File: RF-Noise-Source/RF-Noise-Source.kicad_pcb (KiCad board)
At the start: 2 copper layers, 44 parts, among them J1 Conn_01x02_Male, J2 Conn_Coaxial, Q1 J310, Q2 J310, U1 OPA842xDBV, U2 OPA842xDBV, U3 OPA842xDBV, U4 TPS76350

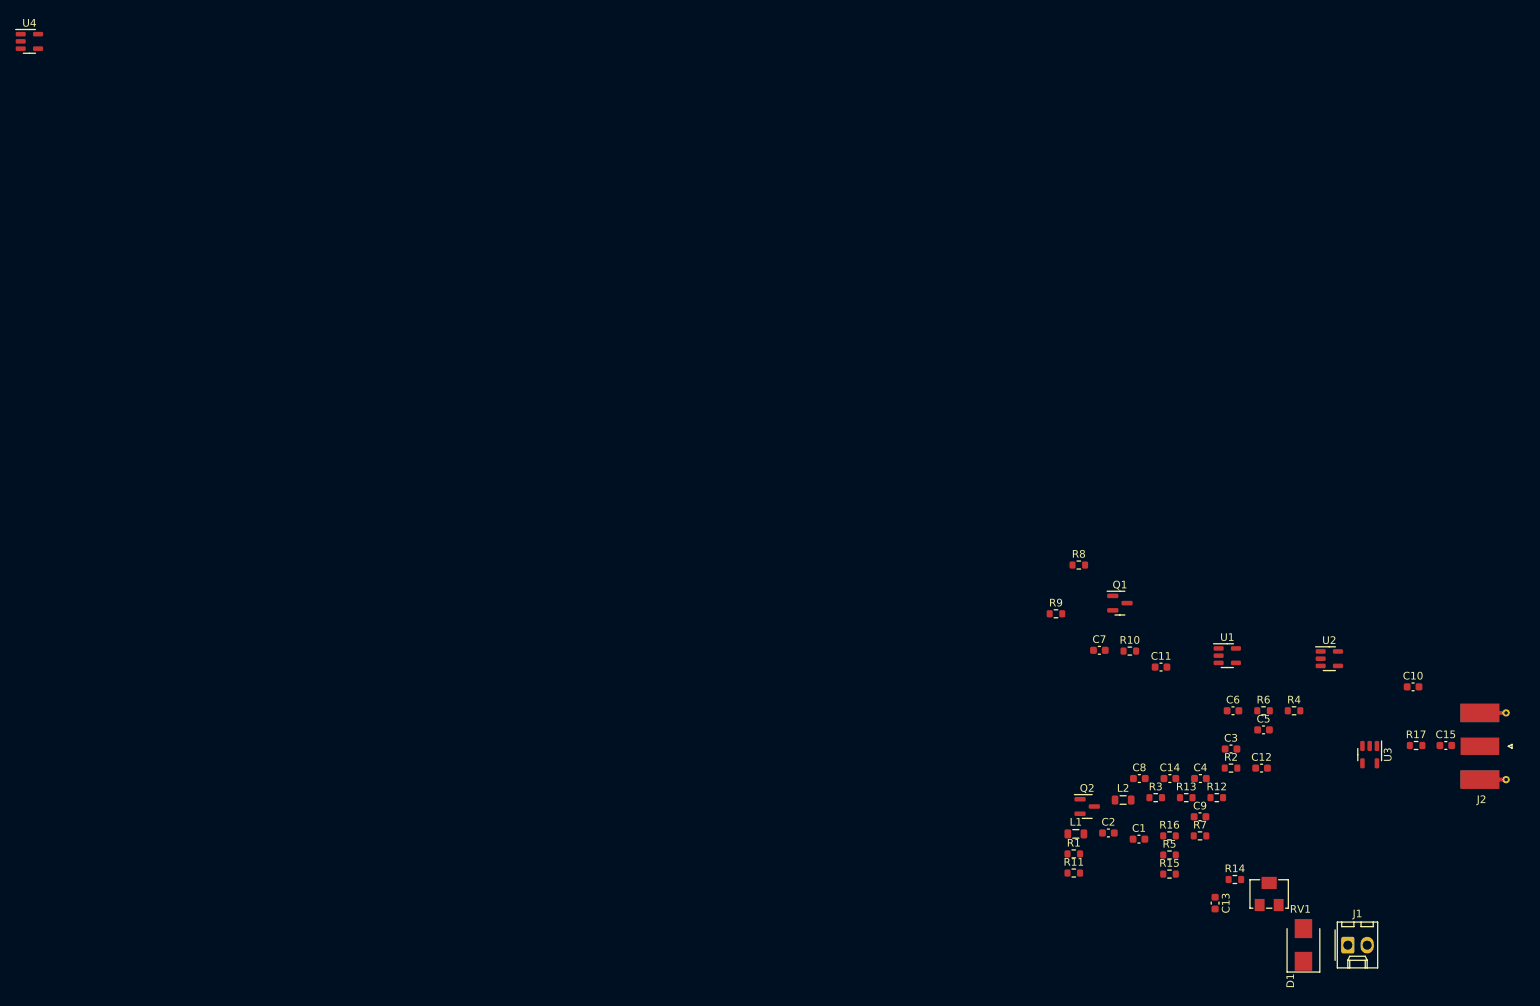
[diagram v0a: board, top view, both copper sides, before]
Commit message: preliminary PCB layout begun, basic blocking complete with some issues regarding signal routing.
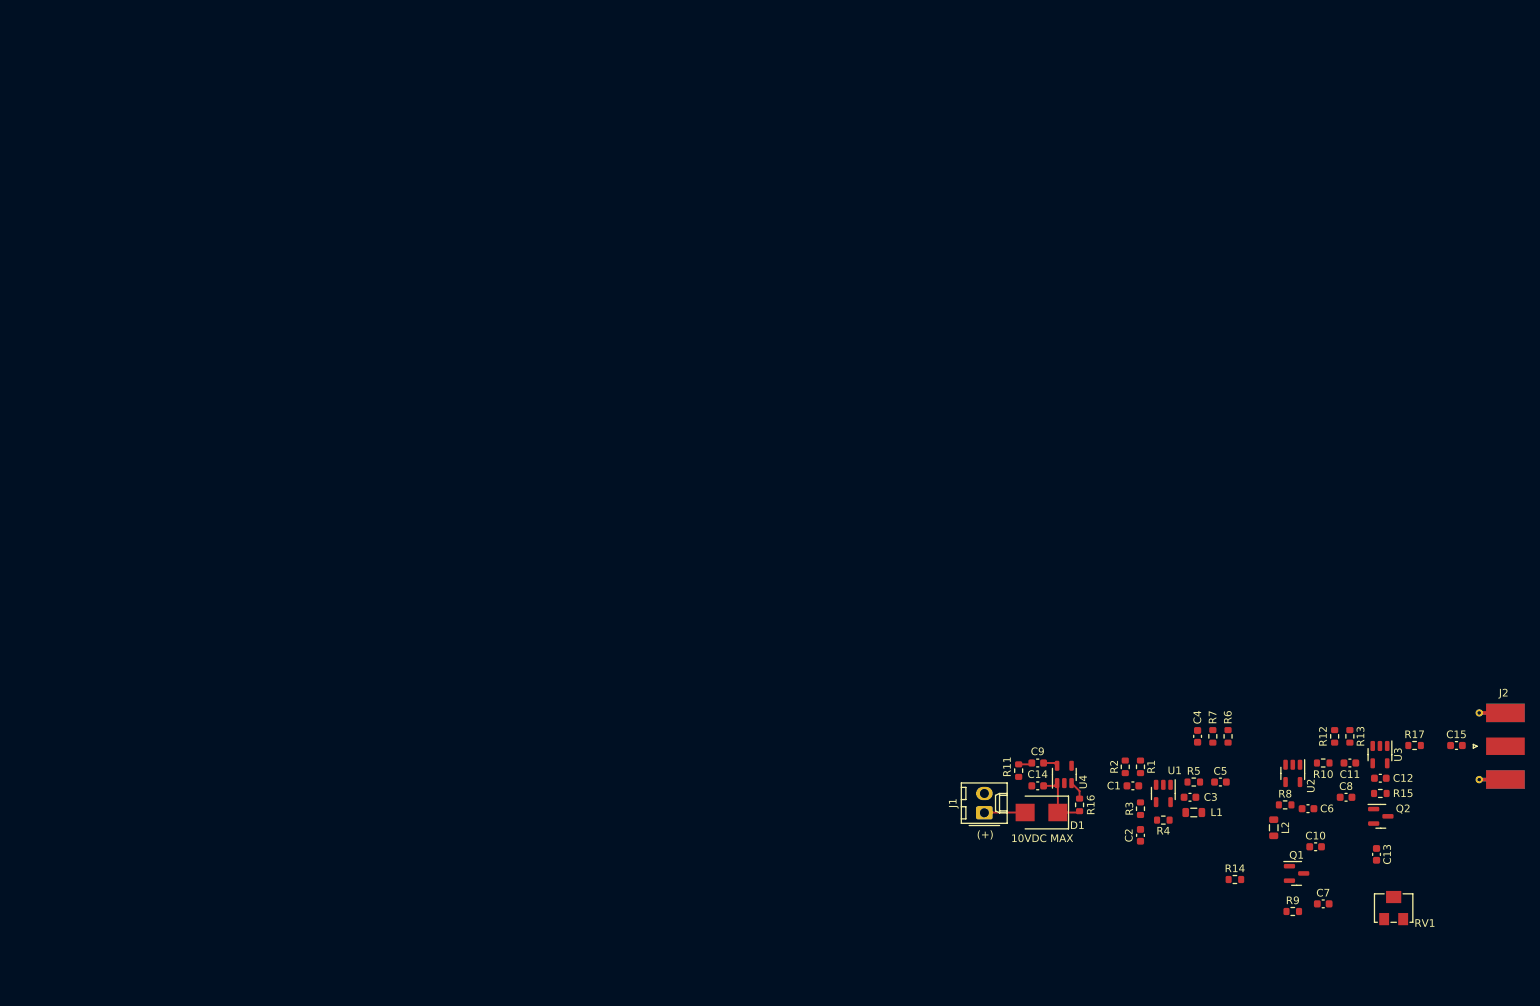
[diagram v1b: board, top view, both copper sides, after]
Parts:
- moved U4 166.6 mm to (138.0, 98.0), turned to 90 degrees
- moved J1 50.8 mm to (127.5, 103.0), turned to 90 degrees
- moved R9 50.0 mm to (168.0, 116.0)
- moved C7 44.4 mm to (172.0, 115.0)
- moved Q1 42.4 mm to (168.5, 111.0)
- moved R8 41.6 mm to (167.0, 102.0)
- moved Q2 38.6 mm to (179.6, 103.5)
- moved D1 38.6 mm to (135.0, 103.0), turned to 180 degrees
- moved R15 29.6 mm to (179.5, 100.5)
- moved R10 29.3 mm to (172.0, 96.5)
- moved C11 27.8 mm to (175.5, 96.5)
- moved C8 27.3 mm to (175.0, 101.0)
- moved C10 24.6 mm to (171.0, 107.5)
- moved R13 22.9 mm to (175.5, 93.0), turned to -90 degrees
- moved C9 22.5 mm to (134.5, 96.5), turned to 180 degrees
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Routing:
- net Net-(D1-K): track 0.00 -> 8.75 mm
- net Net-(D1-A): track 0.00 -> 5.37 mm
- net Net-(U4-EN): track 0.00 -> 2.47 mm
- net +5V: track 0.00 -> 1.93 mm
- net Net-(C9-Pad2): track 0.00 -> 1.80 mm
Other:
- board text added: "(+)"
- board text added: "10VDC MAX"
